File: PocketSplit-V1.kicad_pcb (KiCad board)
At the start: 2 copper layers, 85.9 x 48.8 mm, 61 parts, among them J1 4PIN, SW1 SW_THT_6x6, SW10 SW_THT_6x6, SW11 SW_THT_6x6, SW12 SW_THT_6x6, SW13 SW_THT_6x6, SW14 SW_THT_6x6, SW15 SW_THT_6x6, SW16 SW_THT_6x6, SW17 SW_THT_6x6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

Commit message: PCB updates
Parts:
- added ?: , , F.Cu at (53.3, 84.3)
- added ?: , , F.Cu at (76.5, 43.4)
- added ?: , , F.Cu at (103.1, 57.1)
- added ?: , , F.Cu at (103.1, 74.4)
- added ?: , , F.Cu at (34.5, 54.6)
- moved RST1 1.27 mm to (105.4, 63.2)
- moved J1 1.05 mm to (106.3, 42.6)
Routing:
- net RST: track 27.5 -> 29.5 mm
- net DATA: track 25.9 -> 27.0 mm
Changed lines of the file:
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@@
     )
+  )
+  (footprint "" (layer "F.Cu")
+    (at 53.34 84.328)
+    (fp_text reference "" (at 0 0) (layer "F.SilkS")
+      (effects (font (size 1.27 1.27) (thickness 0.15)))
+    )
+    (fp_text value "" (at 0 0) (layer "F.SilkS")
+      (effects (font (size 1.27 1.27) (thickness 0.15)))
+    )
+    (pad "" np_thru_hole circle (at 0 0) (size 2.2 2.2) (drill 2.2) (layers F&B.Cu *.Mask))
   )
   (footprint "Keebio:Switch_THT_6x6x8.5" (layer "F.Cu")
@@
     )
   )
+  (footprint "" (layer "F.Cu")
+    (at 76.454 43.434)
+    (fp_text reference "" (at 0 0) (layer "F.SilkS")
+      (effects (font (size 1.27 1.27) (thickness 0.15)))
+    )
+    (fp_text value "" (at 0 0) (layer "F.SilkS")
+      (effects (font (size 1.27 1.27) (thickness 0.15)))
+    )
+    (pad "" np_thru_hole circle (at 0 0) (size 2.2 2.2) (drill 2.2) (layers F&B.Cu *.Mask))
+  )
   (footprint "Keebio:Switch_THT_6x6x8.5" (layer "F.Cu")
     (at 48.514 84.578)
@@
     )
   )
+  (footprint "" (layer "F.Cu")
+    (at 103.124 57.15)
+    (fp_text reference "" (at 0 0) (layer "F.SilkS")
+      (effects (font (size 1.27 1.27) (thickness 0.15)))
+    )
+    (fp_text value "" (at 0 0) (layer "F.SilkS")
+      (effects (font (size 1.27 1.27) (thickness 0.15)))
+    )
+    (pad "" np_thru_hole circle (at 0 0) (size 2.2 2.2) (drill 2.2) (layers F&B.Cu *.Mask))
+  )
   (footprint "Keebio:Switch_THT_6x6x8.5" (layer "F.Cu")
     (at 39.116 76.962)
@@
   )
   (footprint "l58:MJ-4PP-9" (layer "F.Cu")
-    (at 106.031 43.5845)
+    (at 106.285 42.5685)
     (property "Sheetfile" "PocketSplit-V1.kicad_sch")
     (property "Sheetname" "")
@@
     )
   )
+  (footprint "" (layer "F.Cu")
+    (at 103.124 74.422)
+    (fp_text reference "" (at 0 0) (layer "F.SilkS")
+      (effects (font (size 1.27 1.27) (thickness 0.15)))
+    )
+    (fp_text value "" (at 0 0) (layer "F.SilkS")
+      (effects (font (size 1.27 1.27) (thickness 0.15)))
+    )
+    (pad "" np_thru_hole circle (at 0 0) (size 2.2 2.2) (drill 2.2) (layers F&B.Cu *.Mask))
+  )
   (footprint "Keebio:Switch_THT_6x6x8.5" (layer "F.Cu")
     (at 57.964 74.454)
@@
   )
   (footprint "l58:TACT_SWITCH_TVBP06" (layer "F.Cu")
-    (at 105.41 61.976 90)
+    (at 105.41 63.246 90)
     (property "Sheetfile" "PocketSplit-V1.kicad_sch")
     (property "Sheetname" "")
@@
       (rotate (xyz 0 0 90))
     )
+  )
+  (footprint "" (layer "F.Cu")
+    (at 34.544 54.61)
+    (fp_text reference "" (at 0 0) (layer "F.SilkS")
+      (effects (font (size 1.27 1.27) (thickness 0.15)))
+    )
+    (fp_text value "" (at 0 0) (layer "F.SilkS")
+      (effects (font (size 1.27 1.27) (thickness 0.15)))
+    )
+    (pad "" np_thru_hole circle (at 0 0) (size 2.2 2.2) (drill 2.2) (layers F&B.Cu *.Mask))
   )
   (footprint "l58:Diode_TH_SOD123_Edited" placed (layer "B.Cu")
@@
   (segment (start 97.632975 51.487745) (end 98.82872 50.292) (width 0.15) (layer "F.Cu") (net 15))
   (segment (start 84.887535 51.487745) (end 97.632975 51.487745) (width 0.15) (layer "F.Cu") (net 15))
-  (segment (start 101.346 56.09975) (end 103.97225 58.726) (width 0.15) (layer "B.Cu") (net 15))
-  (segment (start 101.346 51.054) (end 101.346 56.09975) (width 0.15) (layer "B.Cu") (net 15))
+  (segment (start 102.668 59.996) (end 105.41 59.996) (width 0.15) (layer "B.Cu") (net 15))
+  (segment (start 98.82872 50.292) (end 100.584 50.292) (width 0.15) (layer "B.Cu") (net 15))
   (segment (start 100.584 50.292) (end 101.346 51.054) (width 0.15) (layer "B.Cu") (net 15))
-  (segment (start 103.97225 58.726) (end 105.41 58.726) (width 0.15) (layer "B.Cu") (net 15))
-  (segment (start 98.82872 50.292) (end 100.584 50.292) (width 0.15) (layer "B.Cu") (net 15))
+  (segment (start 101.346 51.054) (end 101.346 58.674) (width 0.15) (layer "B.Cu") (net 15))
+  (segment (start 101.346 58.674) (end 102.668 59.996) (width 0.15) (layer "B.Cu") (net 15))
   (segment (start 97.020208 52.832) (end 83.58872 52.832) (width 0.15) (layer "F.Cu") (net 16))
   (segment (start 97.027999 50.2893) (end 97.025299 50.292) (width 0.15) (layer "F.Cu") (net 16))
@@
   (segment (start 98.300699 51.562) (end 97.027999 50.2893) (width 0.15) (layer "B.Cu") (net 16))
   (segment (start 100.07479 54.102) (end 98.30043 54.102) (width 0.15) (layer "B.Cu") (net 16))
-  (segment (start 102.181 53.8845) (end 101.1285 52.832) (width 0.15) (layer "F.Cu") (net 17))
   (segment (start 101.1285 52.832) (end 98.82872 52.832) (width 0.15) (layer "F.Cu") (net 17))
-  (segment (start 102.181 53.8845) (end 108.131 53.8845) (width 0.15) (layer "F.Cu") (net 17))
+  (segment (start 101.165 52.8685) (end 108.385 52.8685) (width 0.15) (layer "F.Cu") (net 17))
   (segment (start 84.887535 54.027745) (end 97.632975 54.027745) (width 0.15) (layer "F.Cu") (net 17))
   (segment (start 97.632975 54.027745) (end 98.82872 52.832) (width 0.15) (layer "F.Cu") (net 17))
+  (segment (start 101.1285 52.832) (end 101.165 52.8685) (width 0.15) (layer "F.Cu") (net 17))
   (segment (start 83.58872 60.452) (end 97.028 60.452) (width 0.15) (layer "F.Cu") (net 18))
   (via (at 97.028 60.452) (size 0.5) (drill 0.3) (layers "F.Cu" "B.Cu") (net 18))
@@
   (segment (start 98.350745 46.407745) (end 97.155 45.212) (width 0.15) (layer "B.Cu") (net 50))
   (segment (start 83.58872 47.752) (end 97.028 47.752) (width 0.15) (layer "F.Cu") (net 109))
-  (segment (start 102.181 46.8845) (end 102.181 46.89428) (width 0.15) (layer "F.Cu") (net 109))
-  (segment (start 102.181 46.8845) (end 108.131 46.8845) (width 0.15) (layer "F.Cu") (net 109))
-  (segment (start 102.181 46.89428) (end 100.127535 48.947745) (width 0.15) (layer "F.Cu") (net 109))
+  (segment (start 102.435 46.64028) (end 100.127535 48.947745) (width 0.15) (layer "F.Cu") (net 109))
+  (segment (start 108.385 45.8685) (end 102.435 45.8685) (width 0.15) (layer "F.Cu") (net 109))
+  (segment (start 102.435 45.8685) (end 102.435 46.64028) (width 0.15) (layer "F.Cu") (net 109))
   (via (at 97.028 47.752) (size 0.5) (drill 0.3) (layers "F.Cu" "B.Cu") (net 109))
   (segment (start 100.07479 49.022) (end 98.298 49.022) (width 0.15) (layer "B.Cu") (net 109))
   (segment (start 98.298 49.022) (end 97.028 47.752) (width 0.15) (layer "B.Cu") (net 109))
-  (segment (start 103.931 55.3845) (end 106.381 55.3845) (width 0.15) (layer "F.Cu") (net 110))
+  (segment (start 104.185 54.3685) (end 106.635 54.3685) (width 0.25) (layer "F.Cu") (net 110))
   (zone (net 16) (net_name "GND") (layer "F.Cu") (hatch edge 0.508)
     (connect_pads (clearance 0.508))

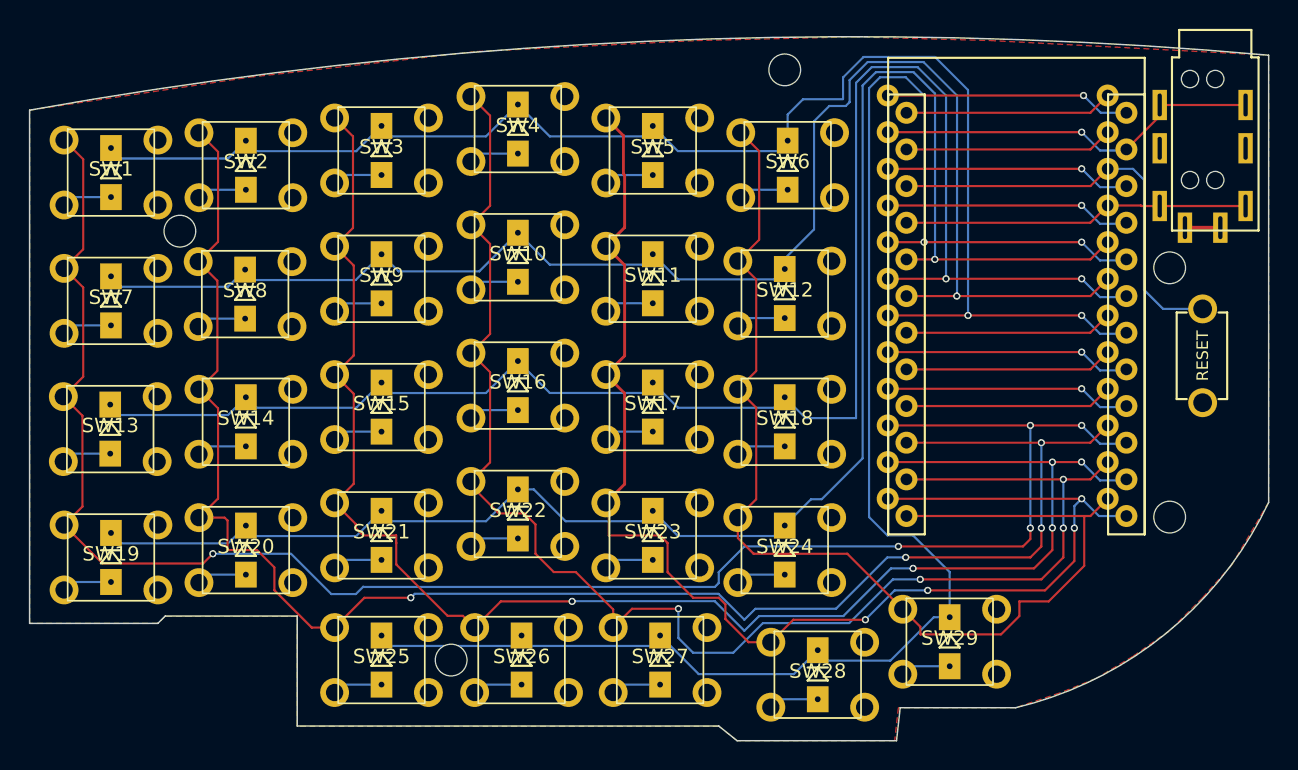
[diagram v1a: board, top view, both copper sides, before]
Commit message: Added M1.4 mounting holes
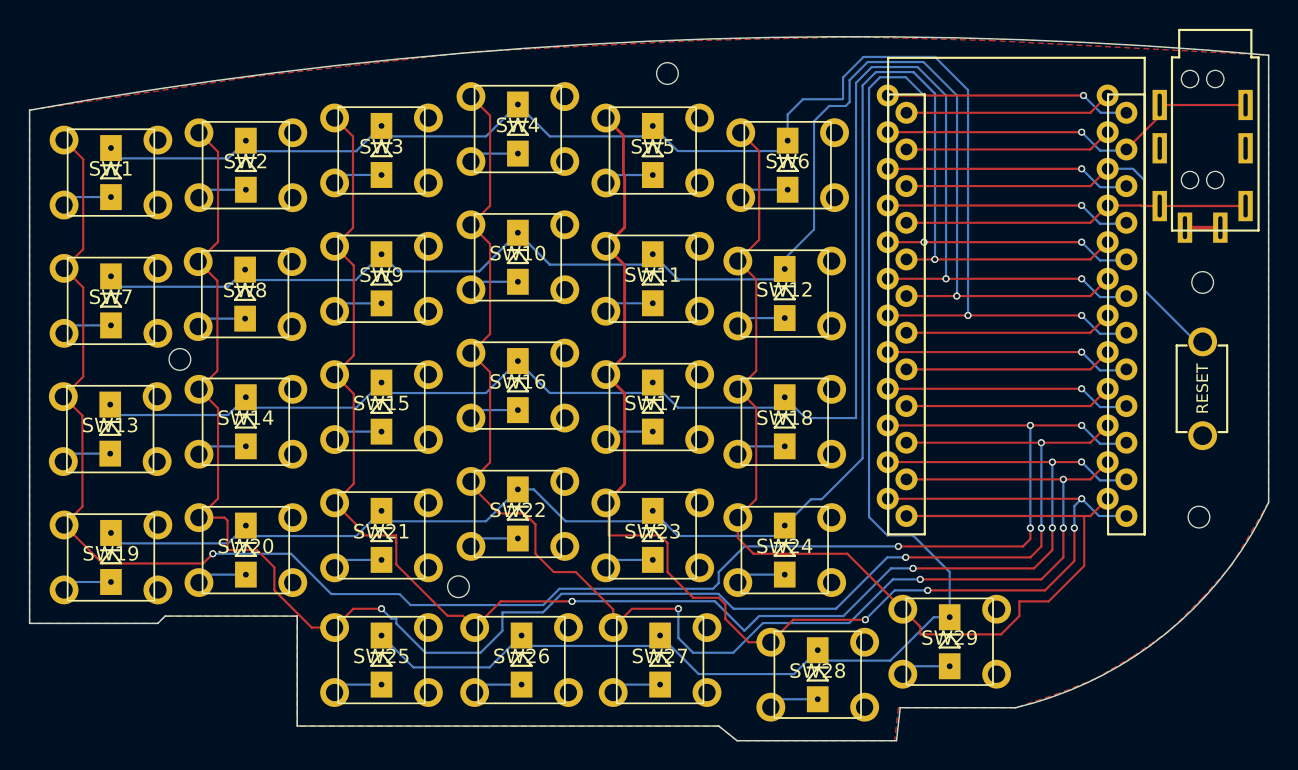
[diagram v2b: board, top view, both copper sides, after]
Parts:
- removed ? (x5): , 
- added H1: MountingHole, MountingHole:MountingHole_2.2mm_M2, F.Cu at (68.3, 43.7)
- added H2: MountingHole, MountingHole:MountingHole_2.2mm_M2, F.Cu at (34.5, 63.5)
- added H3: MountingHole, MountingHole:MountingHole_2.2mm_M2, F.Cu at (53.8, 79.2)
- added H4: MountingHole, MountingHole:MountingHole_2.2mm_M2, F.Cu at (105.2, 74.4)
- added H5: MountingHole, MountingHole:MountingHole_2.2mm_M2, F.Cu at (105.4, 58.2)
- moved RST1 2.29 mm to (105.4, 65.5)
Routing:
- net COL-L-2: track 119.1 -> 121.9 mm
- net ROW-L-5: track 115.8 -> 117.0 mm
- net RST: track 29.5 -> 30.4 mm
- net COL-L-1: track 126.4 -> 127.0 mm
